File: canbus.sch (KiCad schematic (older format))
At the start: 19 parts, among them IC1 MCP25625T-E_ML, IC2 MCP25625T-E_ML, X1 S3D8.000000B20F30T

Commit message: Rename to Sailor Hat
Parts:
- IC1, IC2: symbol pi-supercap-ups:MCP25625T-E_ML -> sailor-hat-rescue:MCP25625T-E_ML-sailor-hat
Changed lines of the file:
@@
-EESchema Schematic File Version 5
-LIBS:pi-supercap-ups-cache
+EESchema Schematic File Version 4
 EELAYER 30 0
 EELAYER END
@@
 Comment3 ""
 Comment4 ""
-Comment5 ""
-Comment6 ""
-Comment7 ""
-Comment8 ""
-Comment9 ""
 $EndDescr
 $Comp
@@
 5V
 $Comp
-L pi-supercap-ups:MCP25625T-E_ML IC1
+L sailor-hat-rescue:MCP25625T-E_ML-sailor-hat IC1
 U 1 1 5D6C6C57
 P 2250 2350
@@
 $EndComp
 $Comp
-L pi-supercap-ups:MCP25625T-E_ML IC2
+L sailor-hat-rescue:MCP25625T-E_ML-sailor-hat IC2
 U 1 1 5D6DDFA9
 P 6950 2250

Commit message: Update licence, tweaks to footprints and ERC
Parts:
- removed IC1, IC2: MCP25625T-E_ML, custom:QFN65P600X600X100-29M-D, symbol sailor-hat-rescue:MCP25625T-E_ML-sailor-hat
- added C22: 100nF, Capacitor_SMD:C_0603_1608Metric_Pad1.05x0.95mm_HandSolder, symbol Device:C
- added U7, U8: MCP25625T-E_ML, QFN65P600X600X100-29M-D, symbol sailor-hat:MCP25625T-E_ML
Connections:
- wire segments 88 -> 92

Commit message: Add a voltage divider for indicating HW version
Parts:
- U7, U8: footprint QFN65P600X600X100-29M-D -> custom:QFN65P600X600X100-29M-D
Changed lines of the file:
@@
 F 0 "U7" H 3400 2750 50  0000 L CNN
 F 1 "MCP25625T-E_ML" H 3400 2650 50  0000 L CNN
-F 2 "QFN65P600X600X100-29M-D" H 3400 2850 50  0001 L CNN
+F 2 "custom:QFN65P600X600X100-29M-D" H 3400 2850 50  0001 L CNN
 F 3 "https://www.mouser.com/datasheet/2/268/20005282B-708896.pdf" H 3400 2750 50  0001 L CNN
 F 4 "Microchip Technology MCP25625T-E/ML, CAN Controller 1Mbit/s CAN 2.0B, 28-Pin QFN" H 3400 2650 50  0001 L CNN "Description"
@@
 F 0 "U8" H 8100 2650 50  0000 L CNN
 F 1 "MCP25625T-E_ML" H 8100 2550 50  0000 L CNN
-F 2 "QFN65P600X600X100-29M-D" H 8100 2750 50  0001 L CNN
+F 2 "custom:QFN65P600X600X100-29M-D" H 8100 2750 50  0001 L CNN
 F 3 "https://www.mouser.com/datasheet/2/268/20005282B-708896.pdf" H 8100 2650 50  0001 L CNN
 F 4 "Microchip Technology MCP25625T-E/ML, CAN Controller 1Mbit/s CAN 2.0B, 28-Pin QFN" H 8100 2550 50  0001 L CNN "Description"

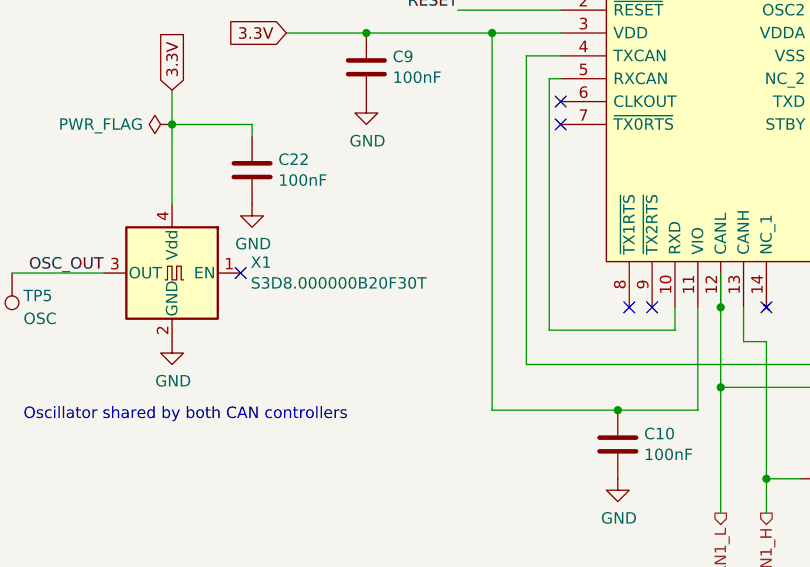
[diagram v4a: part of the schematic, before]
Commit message: Add LCSC part numbers to components
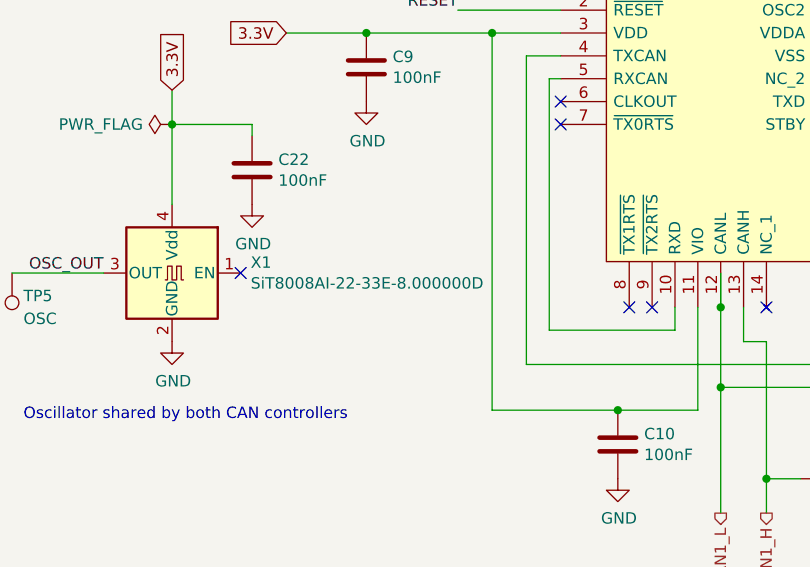
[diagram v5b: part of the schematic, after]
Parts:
- C10, C11, C22, C3, C4, C5, C9: LCSC (none) -> C14663
- R11, R31: LCSC (none) -> C17909
- R21, R24, R25, R29, R30: LCSC (none) -> C25804
- U7, U8: LCSC (none) -> C191253
- X1: value S3D8.000000B20F30T -> SiT8008AI-22-33E-8.000000D; LCSC (none) -> C39097
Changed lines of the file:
@@
 F 4 "" H 3450 4500 50  0001 C CNN "Note"
 F 5 "Min 0.25W" H -3650 2950 50  0001 C CNN "Notes"
+F 6 "C17909" H 3450 4500 50  0001 C CNN "LCSC"
 	1    3450 4500
 	0    1    1    0
@@
 F 2 "Capacitor_SMD:C_0603_1608Metric_Pad1.05x0.95mm_HandSolder" H 1438 2550 50  0001 C CNN
 F 3 "~" H 1400 2700 50  0001 C CNN
+F 4 "C14663" H 1400 2700 50  0001 C CNN "LCSC"
 	1    1400 2700
 	1    0    0    -1
@@
 F 2 "Capacitor_SMD:C_0603_1608Metric_Pad1.05x0.95mm_HandSolder" H 3688 750 50  0001 C CNN
 F 3 "~" H 3650 900 50  0001 C CNN
+F 4 "C14663" H 3650 900 50  0001 C CNN "LCSC"
 	1    3650 900
 	1    0    0    -1
@@
 F 2 "Capacitor_SMD:C_0603_1608Metric_Pad1.05x0.95mm_HandSolder" H 2538 4200 50  0001 C CNN
 F 3 "~" H 2500 4350 50  0001 C CNN
+F 4 "C14663" H 2500 4350 50  0001 C CNN "LCSC"
 	1    2500 4350
 	1    0    0    -1
@@
 F 2 "Resistor_SMD:R_0603_1608Metric_Pad1.05x0.95mm_HandSolder" V 1580 2450 50  0001 C CNN
 F 3 "~" H 1650 2450 50  0001 C CNN
+F 4 "C25804" H 1650 2450 50  0001 C CNN "LCSC"
 	1    1650 2450
 	0    1    1    0
@@
 F 2 "Capacitor_SMD:C_0603_1608Metric_Pad1.05x0.95mm_HandSolder" H 8388 650 50  0001 C CNN
 F 3 "~" H 8350 800 50  0001 C CNN
+F 4 "C14663" H 8350 800 50  0001 C CNN "LCSC"
 	1    8350 800
 	1    0    0    -1
@@
 F 2 "Capacitor_SMD:C_0603_1608Metric_Pad1.05x0.95mm_HandSolder" H 7238 4100 50  0001 C CNN
 F 3 "~" H 7200 4250 50  0001 C CNN
+F 4 "C14663" H 7200 4250 50  0001 C CNN "LCSC"
 	1    7200 4250
 	1    0    0    -1
@@
 F 2 "Capacitor_SMD:C_0603_1608Metric_Pad1.05x0.95mm_HandSolder" H 6138 2450 50  0001 C CNN
 F 3 "~" H 6100 2600 50  0001 C CNN
+F 4 "C14663" H 6100 2600 50  0001 C CNN "LCSC"
 	1    6100 2600
 	1    0    0    -1
@@
 F 4 "" H 8150 4400 50  0001 C CNN "Note"
 F 5 "Min 0.25W" H 1050 2850 50  0001 C CNN "Notes"
+F 6 "C17909" H 8150 4400 50  0001 C CNN "LCSC"
 	1    8150 4400
 	0    1    1    0
@@
 F 2 "Resistor_SMD:R_0603_1608Metric_Pad1.05x0.95mm_HandSolder" V 2880 1150 50  0001 C CNN
 F 3 "~" H 2950 1150 50  0001 C CNN
+F 4 "C25804" H 2950 1150 50  0001 C CNN "LCSC"
 	1    2950 1150
 	1    0    0    -1
@@
 F 2 "Resistor_SMD:R_0603_1608Metric_Pad1.05x0.95mm_HandSolder" V 1480 1900 50  0001 C CNN
 F 3 "~" H 1550 1900 50  0001 C CNN
+F 4 "C25804" H 1550 1900 50  0001 C CNN "LCSC"
 	1    1550 1900
 	1    0    0    -1
@@
 F 2 "Resistor_SMD:R_0603_1608Metric_Pad1.05x0.95mm_HandSolder" V 7580 1050 50  0001 C CNN
 F 3 "~" H 7650 1050 50  0001 C CNN
+F 4 "C25804" H 7650 1050 50  0001 C CNN "LCSC"
 	1    7650 1050
 	1    0    0    -1
@@
 F 2 "Resistor_SMD:R_0603_1608Metric_Pad1.05x0.95mm_HandSolder" V 6180 1800 50  0001 C CNN
 F 3 "~" H 6250 1800 50  0001 C CNN
+F 4 "C25804" H 6250 1800 50  0001 C CNN "LCSC"
 	1    6250 1800
 	1    0    0    -1
@@
 P 5250 3500
 F 0 "X1" H 4906 3546 50  0000 R CNN
-F 1 "S3D8.000000B20F30T" H 4906 3455 50  0000 R CNN
+F 1 "SiT8008AI-22-33E-8.000000D" H 4906 3455 50  0000 R CNN
 F 2 "Oscillator:Oscillator_SMD_Abracon_ASE-4Pin_3.2x2.5mm" H 5950 3150 50  0001 C CNN
 F 3 "http://www.abracon.com/Oscillators/ASV.pdf" H 5150 3500 50  0001 C CNN
+F 4 "C39097" H 5250 3500 50  0001 C CNN "LCSC"
 	1    5250 3500
 	-1   0    0    -1
@@
 F 2 "Capacitor_SMD:C_0603_1608Metric_Pad1.05x0.95mm_HandSolder" H 5638 2900 50  0001 C CNN
 F 3 "~" H 5600 3050 50  0001 C CNN
+F 4 "C14663" H 5600 3050 50  0001 C CNN "LCSC"
 	1    5600 3050
 	1    0    0    -1
@@
 F 12 "70568355" H 3400 1850 50  0001 L CNN "Allied_Number"
 F 13 "https://www.alliedelec.com/microchiptechnologyinc-mcp25625t-e-ml/70568355/" H 3400 1750 50  0001 L CNN "Allied Price/Stock"
+F 14 "C191253" H 2250 2350 50  0001 C CNN "LCSC"
 	1    2250 2350
 	1    0    0    -1
@@
 F 12 "70568355" H 8100 1750 50  0001 L CNN "Allied_Number"
 F 13 "https://www.alliedelec.com/microchiptechnologyinc-mcp25625t-e-ml/70568355/" H 8100 1650 50  0001 L CNN "Allied Price/Stock"
+F 14 "C191253" H 6950 2250 50  0001 C CNN "LCSC"
 	1    6950 2250
 	1    0    0    -1

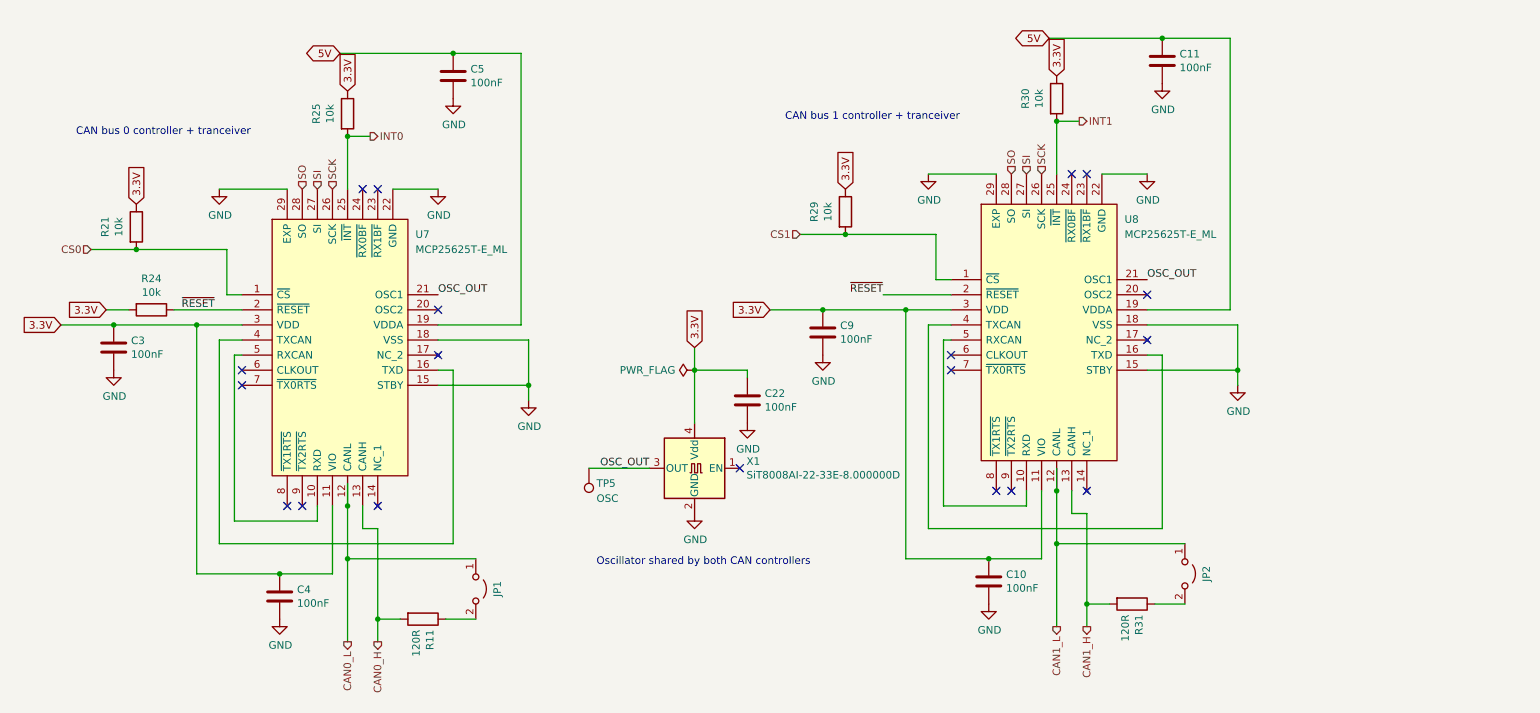
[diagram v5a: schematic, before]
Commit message: Isolated CAN bus implementation
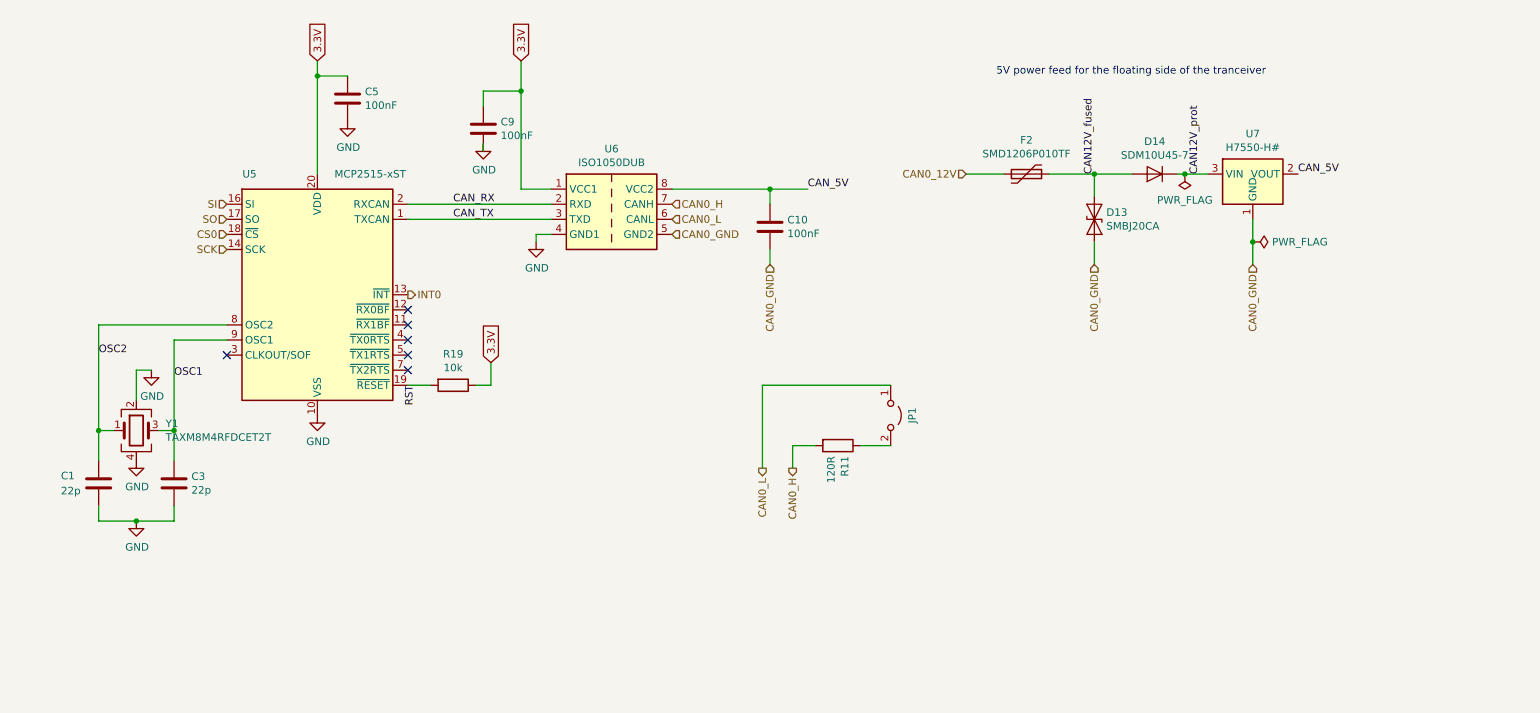
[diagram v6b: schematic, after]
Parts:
- removed C11, C22, C4: 100nF, Capacitor_SMD:C_0603_1608Metric_Pad1.05x0.95mm_HandSolder, symbol Device:C
- removed JP2: Term, Connector_PinHeader_2.54mm:PinHeader_1x02_P2.54mm_Vertical, symbol Jumper:Jumper_2_Open
- removed R21, R24, R25, R29, R30: 10k, Resistor_SMD:R_0603_1608Metric_Pad1.05x0.95mm_HandSolder, symbol Device:R
- removed R31: 120R, Resistor_SMD:R_1206_3216Metric_Pad1.42x1.75mm_HandSolder, symbol Device:R
- removed TP5: OSC, TestPoint:TestPoint_Keystone_5000-5004_Miniature, symbol Connector:TestPoint
- removed U7, U8: MCP25625T-E_ML, custom:QFN65P600X600X100-29M-D, symbol sailor-hat:MCP25625T-E_ML
- removed X1: SiT8008AI-22-33E-8.000000D, Oscillator:Oscillator_SMD_Abracon_ASE-4Pin_3.2x2.5mm, symbol Oscillator:ASE-xxxMHz
- added C1: 22p, Capacitor_SMD:C_0603_1608Metric, symbol Device:C
- added D13: SMBJ20CA, Diode_SMD:D_SMB, symbol Device:D_TVS
- added D14: SDM10U45-7, Diode_SMD:D_SOD-523, symbol Device:D
- added F2: SMD1206P010TF, Fuse:Fuse_1206_3216Metric, symbol Device:Polyfuse
- added R19: 10k, Resistor_SMD:R_0603_1608Metric, symbol Device:R
- added U5: MCP2515-xST, Package_SO:TSSOP-20_4.4x6.5mm_P0.65mm, symbol Interface_CAN_LIN:MCP2515-xST
- added U6: ISO1050DUB, Package_SO:SOP-8_6.62x9.15mm_P2.54mm, symbol Interface_CAN_LIN:ISO1050DUB
- added U7: H7550-H#, Package_TO_SOT_SMD:SOT-23, symbol sailor-hat:HT75xx-1-SOT23
- added Y1: TAXM8M4RFDCET2T, Crystal:Crystal_SMD_3225-4Pin_3.2x2.5mm, symbol Device:Crystal_GND24
- C10, C5, C9: footprint Capacitor_SMD:C_0603_1608Metric_Pad1.05x0.95mm_HandSolder -> Capacitor_SMD:C_0603_1608Metric
- C3: value 100nF -> 22p; footprint Capacitor_SMD:C_0603_1608Metric_Pad1.05x0.95mm_HandSolder -> Capacitor_SMD:C_0603_1608Metric; LCSC C14663 -> (none)
- R11: footprint Resistor_SMD:R_1206_3216Metric_Pad1.42x1.75mm_HandSolder -> Resistor_SMD:R_1206_3216Metric
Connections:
- net 5V is gone; now on net 3.3V: C5.1
- net 3.3V: now also R19.1, U5.20 (VDD), U6.1 (VCC1); no longer C10.1, C3.1
- net CAN0_H: now also U6.7 (CANH)
- net CAN0_L: now also U6.6 (CANL)
- net CS0: now also U5.18 (~CS)
- net GND: now also C1.2, U5.10 (VSS), U6.4 (GND1), Y1.2, Y1.4; no longer C10.2
- net INT0: now also U5.13 (~INT)
- net SCK: now also U5.14 (SCK)
- net SI: now also U5.16 (SI)
- net SO: now also U5.17 (SO)
- new net CAN0_12V: F2.2
- new net CAN0_GND: C10.2, D13.2 (A2), U6.5 (GND2), U7.1 (GND)
- new net CAN12V_fused: D13.1 (A1), D14.2 (A), F2.1
- new net CAN12V_prot: D14.1 (K), U7.3 (VIN)
- new net CAN_5V: C10.1, U6.8 (VCC2), U7.2 (VOUT)
- new net CAN_RX: U5.2 (RXCAN), U6.2 (RXD)
- new net CAN_TX: U5.1 (TXCAN), U6.3 (TXD)
- new net OSC1: C3.1, U5.9 (OSC1), Y1.3
- new net OSC2: C1.1, U5.8 (OSC2), Y1.1
- new net RST: R19.2, U5.19 (~RESET)
- no-connect marks 19 -> 6
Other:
- note added: "5V power feed for the floating side of the tranceiver"
- note removed: "CAN bus 0 controller + tranceiver"
- note removed: "CAN bus 1 controller + tranceiver"
- note removed: "Oscillator shared by both CAN controllers"
- moved on the sheet: JP1, R11

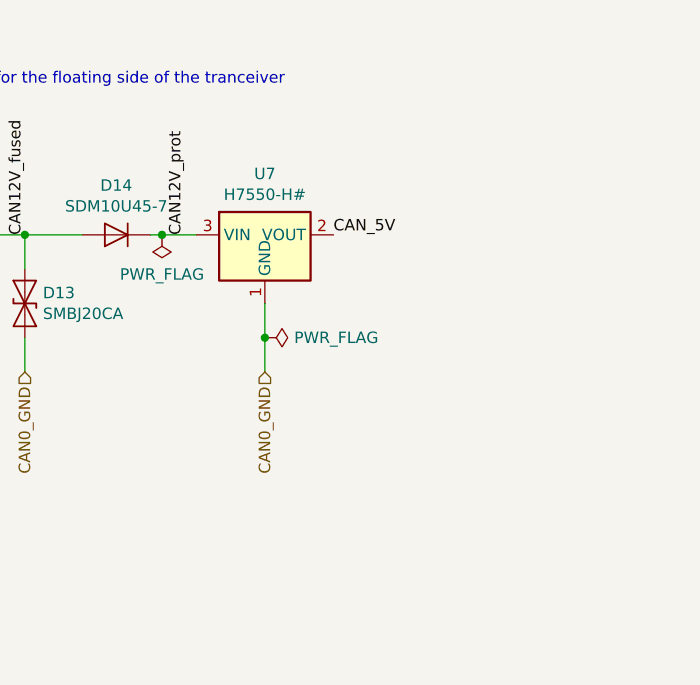
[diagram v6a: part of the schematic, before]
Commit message: Optimize PCB layout; add missing filter caps
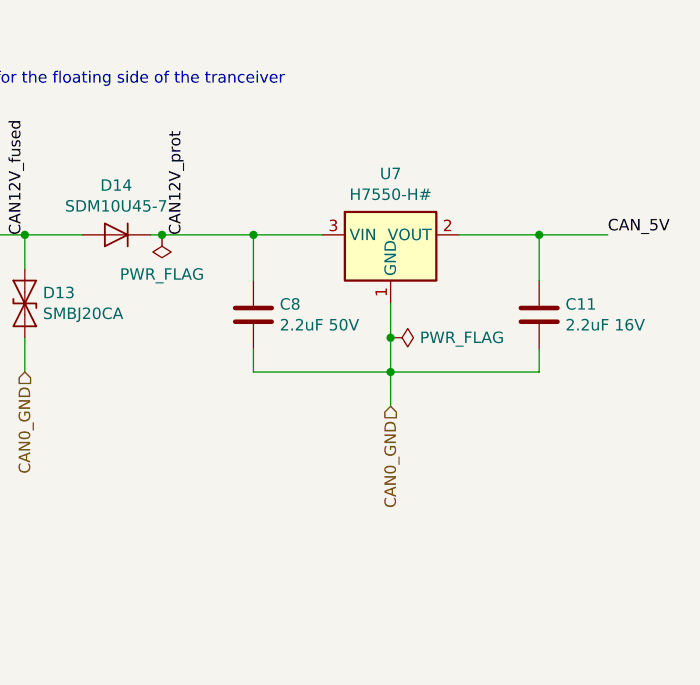
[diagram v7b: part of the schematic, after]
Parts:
- added C11: 2.2uF 16V, Capacitor_SMD:C_0603_1608Metric, symbol Device:C
- added C8: 2.2uF 50V, Capacitor_SMD:C_1206_3216Metric, symbol Device:C
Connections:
- net CAN0_GND: now also C11.2, C8.2
- net CAN12V_prot: now also C8.1
- net CAN_5V: now also C11.1
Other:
- moved on the sheet: U7
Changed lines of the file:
@@
 L sailor-hat:HT75xx-1-SOT23 U7
 U 1 1 5F3E4347
-P 8950 1650
-F 0 "U7" H 8950 2017 50  0000 C CNN
-F 1 "H7550-H#" H 8950 1926 50  0000 C CNN
-F 2 "Package_TO_SOT_SMD:SOT-23" H 8950 1975 50  0001 C CIN
-F 3 "https://www.holtek.com/documents/10179/116711/HT75xx-1v250.pdf" H 8950 1750 50  0001 C CNN
-	1    8950 1650
+P 9500 1650
+F 0 "U7" H 9500 2017 50  0000 C CNN
+F 1 "H7550-H#" H 9500 1926 50  0000 C CNN
+F 2 "Package_TO_SOT_SMD:SOT-23" H 9500 1975 50  0001 C CIN
+F 3 "" H 9500 1750 50  0001 C CNN
+	1    9500 1650
 	1    0    0    -1
 $EndComp
@@
 	8450 1550 8500 1550
 Wire Wire Line
-	8950 2150 8950 2000
+	9500 2300 9500 2150
 Wire Wire Line
 	7900 1700 7900 1550
@@
 Wire Wire Line
 	7900 2000 7900 2150
-Text Label 9250 1550 0    50   ~ 0
+Text Label 10450 1550 0    50   ~ 0
 CAN_5V
 Text Label 6000 1650 0    50   ~ 0
@@
 Text HLabel 5100 1950 2    50   Input ~ 0
 CAN0_GND
-Text HLabel 8950 2150 3    50   Input ~ 0
+Text HLabel 9500 2300 3    50   Input ~ 0
 CAN0_GND
 Wire Wire Line
@@
 Connection ~ 8500 1550
 Wire Wire Line
-	8500 1550 8650 1550
+	8500 1550 8900 1550
 $Comp
 L power:PWR_FLAG #FLG0108
 U 1 1 5F4B190A
-P 8950 2000
-F 0 "#FLG0108" H 8950 2075 50  0001 C CNN
-F 1 "PWR_FLAG" V 8950 2128 50  0000 L CNN
-F 2 "" H 8950 2000 50  0001 C CNN
-F 3 "~" H 8950 2000 50  0001 C CNN
-	1    8950 2000
+P 9500 2000
+F 0 "#FLG0108" H 9500 2075 50  0001 C CNN
+F 1 "PWR_FLAG" V 9500 2128 50  0000 L CNN
+F 2 "" H 9500 2000 50  0001 C CNN
+F 3 "~" H 9500 2000 50  0001 C CNN
+	1    9500 2000
 	0    1    1    0
 $EndComp
-Connection ~ 8950 2000
-Wire Wire Line
-	8950 2000 8950 1850
+Connection ~ 9500 2000
+Wire Wire Line
+	9500 2000 9500 1850
 Text Label 3650 1750 0    50   ~ 0
 CAN_RX
@@
 Text HLabel 5750 2150 3    50   Input ~ 0
 CAN0_GND
+$Comp
+L Device:C C?
+U 1 1 5F3C81F3
+P 8900 1900
+AR Path="/5CA65CC5/5F3C81F3" Ref="C?"  Part="1"
+AR Path="/5C348474/5F3C81F3" Ref="C8"  Part="1"
+F 0 "C8" H 9015 1946 50  0000 L CNN
+F 1 "2.2uF 50V" H 9015 1855 50  0000 L CNN
+F 2 "Capacitor_SMD:C_1206_3216Metric" H 8938 1750 50  0001 C CNN
+F 3 "~" H 8900 1900 50  0001 C CNN
+F 4 "C50254" H 8900 1900 50  0001 C CNN "LCSC"
+	1    8900 1900
+	1    0    0    -1
+$EndComp
+$Comp
+L Device:C C?
+U 1 1 5F3C9CED
+P 10150 1900
+AR Path="/5CA65CC5/5F3C9CED" Ref="C?"  Part="1"
+AR Path="/5C348474/5F3C9CED" Ref="C11"  Part="1"
+F 0 "C11" H 10265 1946 50  0000 L CNN
+F 1 "2.2uF 16V" H 10265 1855 50  0000 L CNN
+F 2 "Capacitor_SMD:C_0603_1608Metric" H 10188 1750 50  0001 C CNN
+F 3 "~" H 10150 1900 50  0001 C CNN
+F 4 "C23630" H 10150 1900 50  0001 C CNN "LCSC"
+	1    10150 1900
+	1    0    0    -1
+$EndComp
+Wire Wire Line
+	8900 1750 8900 1550
+Connection ~ 8900 1550
+Wire Wire Line
+	8900 1550 9200 1550
+Wire Wire Line
+	10150 1750 10150 1550
+Wire Wire Line
+	10150 1550 9800 1550
+Wire Wire Line
+	10450 1550 10150 1550
+Connection ~ 10150 1550
+Wire Wire Line
+	8900 2050 8900 2150
+Wire Wire Line
+	8900 2150 9500 2150
+Connection ~ 9500 2150
+Wire Wire Line
+	9500 2150 9500 2000
+Wire Wire Line
+	9500 2150 10150 2150
+Wire Wire Line
+	10150 2150 10150 2050
 $EndSCHEMATC
